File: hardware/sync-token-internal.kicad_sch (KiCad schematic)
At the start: 6 parts, among them U1 74AHC74D,118, U2 SN74LV1T125DBVRG4, U3 SN74LV1T125DBVRG4

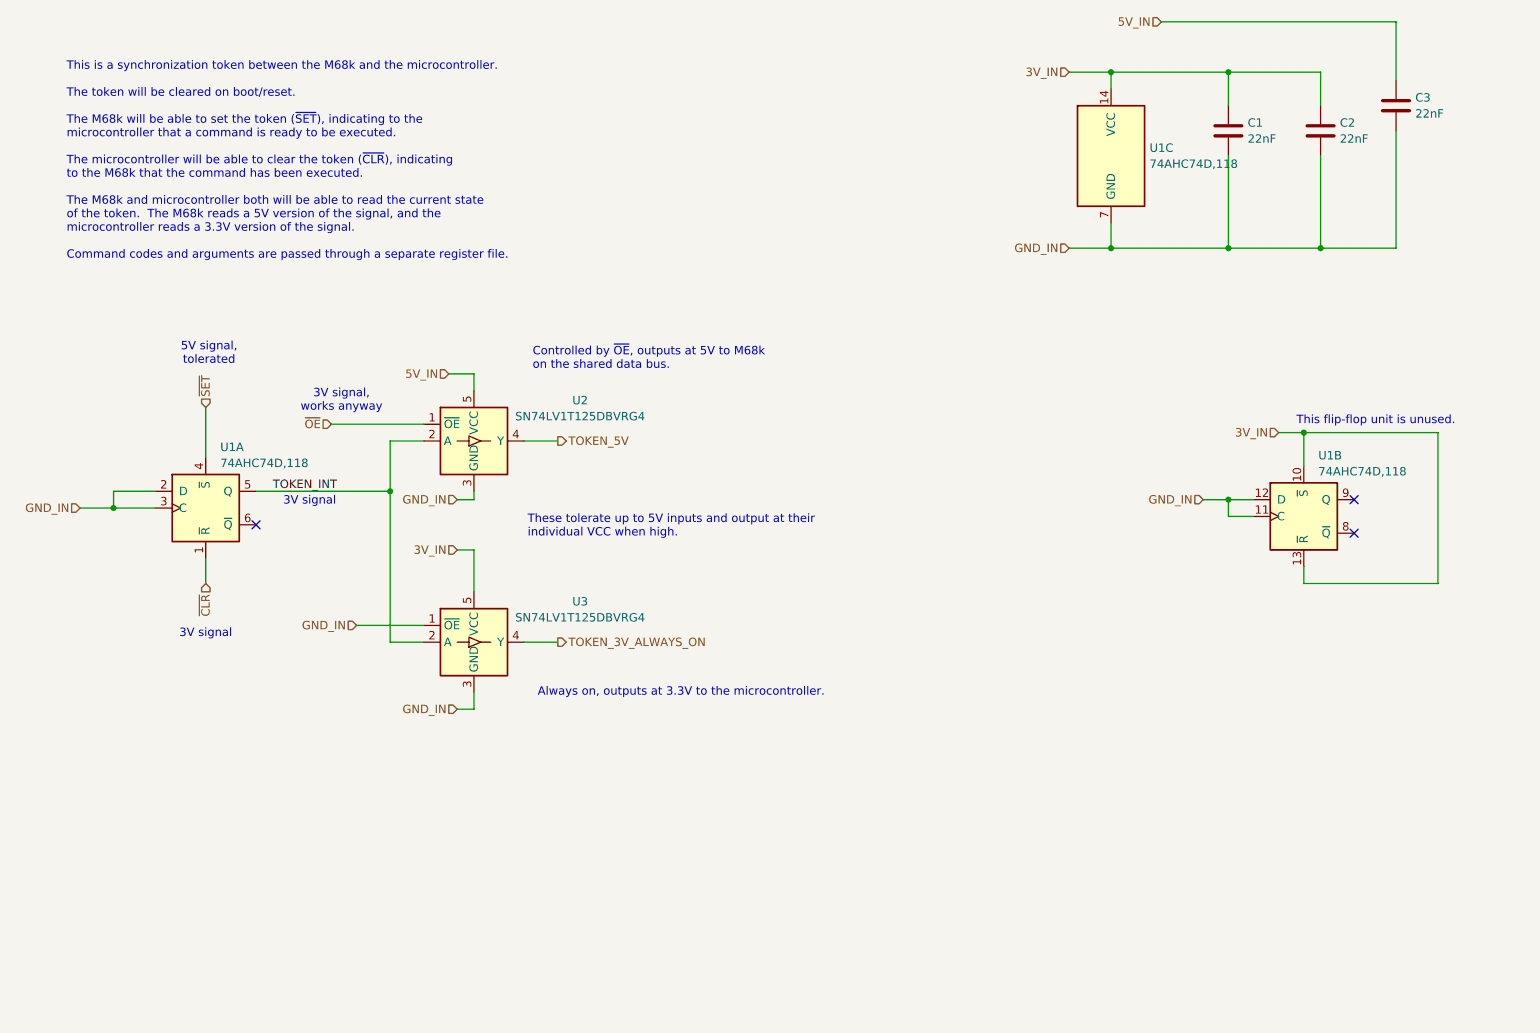
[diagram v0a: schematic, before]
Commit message: Massively reorganize board designs
Now planning to have most assembly done by JLCPCB, so trace sizes,
part selections, etc. are set accordingly.

New boards are:
 - cartridge interface & flash
 - microcontroller & registers
 - sram x2
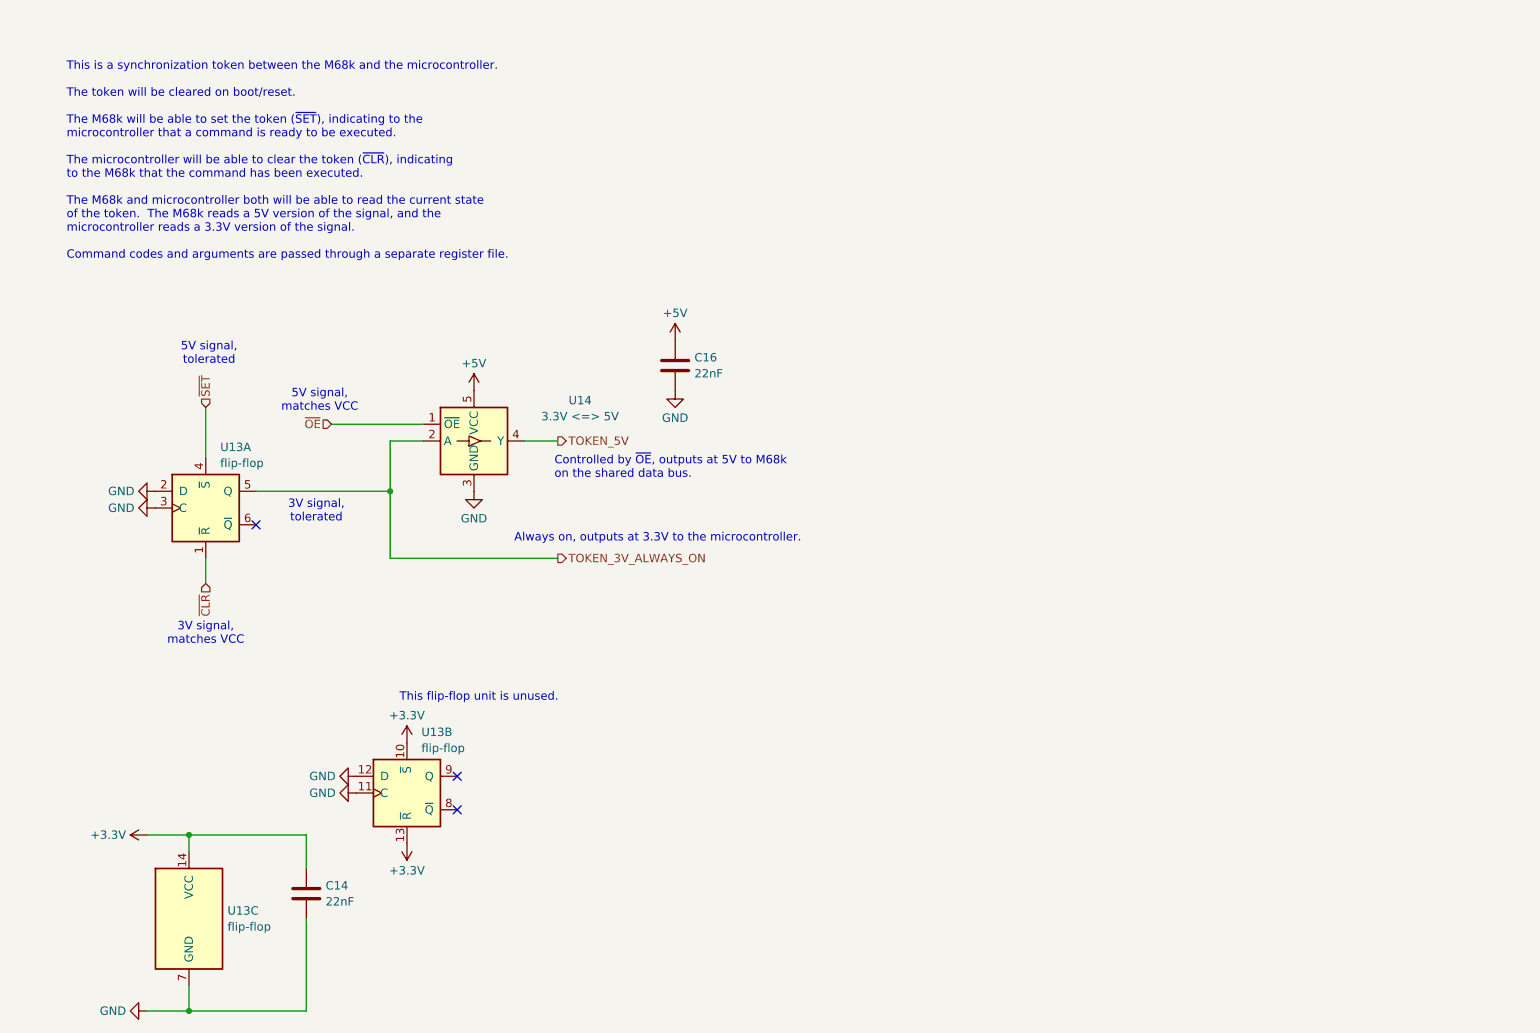
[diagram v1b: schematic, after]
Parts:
- removed C2: 22nF, Capacitor_SMD:C_0603_1608Metric, symbol Device:C
- removed U3: SN74LV1T125DBVRG4, Package_TO_SOT_SMD:SOT-23-5, symbol Logic_LevelTranslator:SN74LV1T125DBV
- C14: renamed from C1; JLCPCB Part Number (none) -> C21122; Mouser Part Number (none) -> 187-CL10B223KB8NNNC; Part Number (none) -> CL10B223KB8NNNC
- C16: renamed from C3; JLCPCB Part Number (none) -> C21122; Mouser Part Number (none) -> 187-CL10B223KB8NNNC; Part Number (none) -> CL10B223KB8NNNC
- U13: renamed from U1; value 74AHC74D,118 -> flip-flop; footprint Package_SO:SO-14_3.9x8.65mm_P1.27mm -> Package_SO:TSSOP-14_4.4x5mm_P0.65mm; JLCPCB Part Number (none) -> C71900; Mouser Part Number (none) -> 771-AHCPW118; Part Number (none) -> 74AHC74PW,118
- U14: renamed from U2; value SN74LV1T125DBVRG4 -> 3.3V <=> 5V; JLCPCB Part Number (none) -> C2675706; Mouser Part Number (none) -> 595-74LV1T125DBVRG4; Part Number (none) -> SN74LV1T125DBVRG4
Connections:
- net TOKEN_INT is gone; now on net TOKEN_3V_ALWAYS_ON: U13.5 (Q), U14.2 (A)
- net 3V_IN renamed +3.3V
- net 5V_IN renamed +5V
- net GND_IN renamed GND
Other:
- note added: "3V signal, matches VCC"
- note added: "3V signal, tolerated"
- note added: "5V signal, matches VCC"
- note removed: "3V signal"
- note removed: "3V signal, works anyway"
- note removed: "These tolerate up to 5V inputs and output at their individual VCC when high."
- moved on the sheet: C14, C16, U13B, U13C

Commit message: Add second sync bit to flag errors back to the Sega
Also split firmware speed tests out into their own file
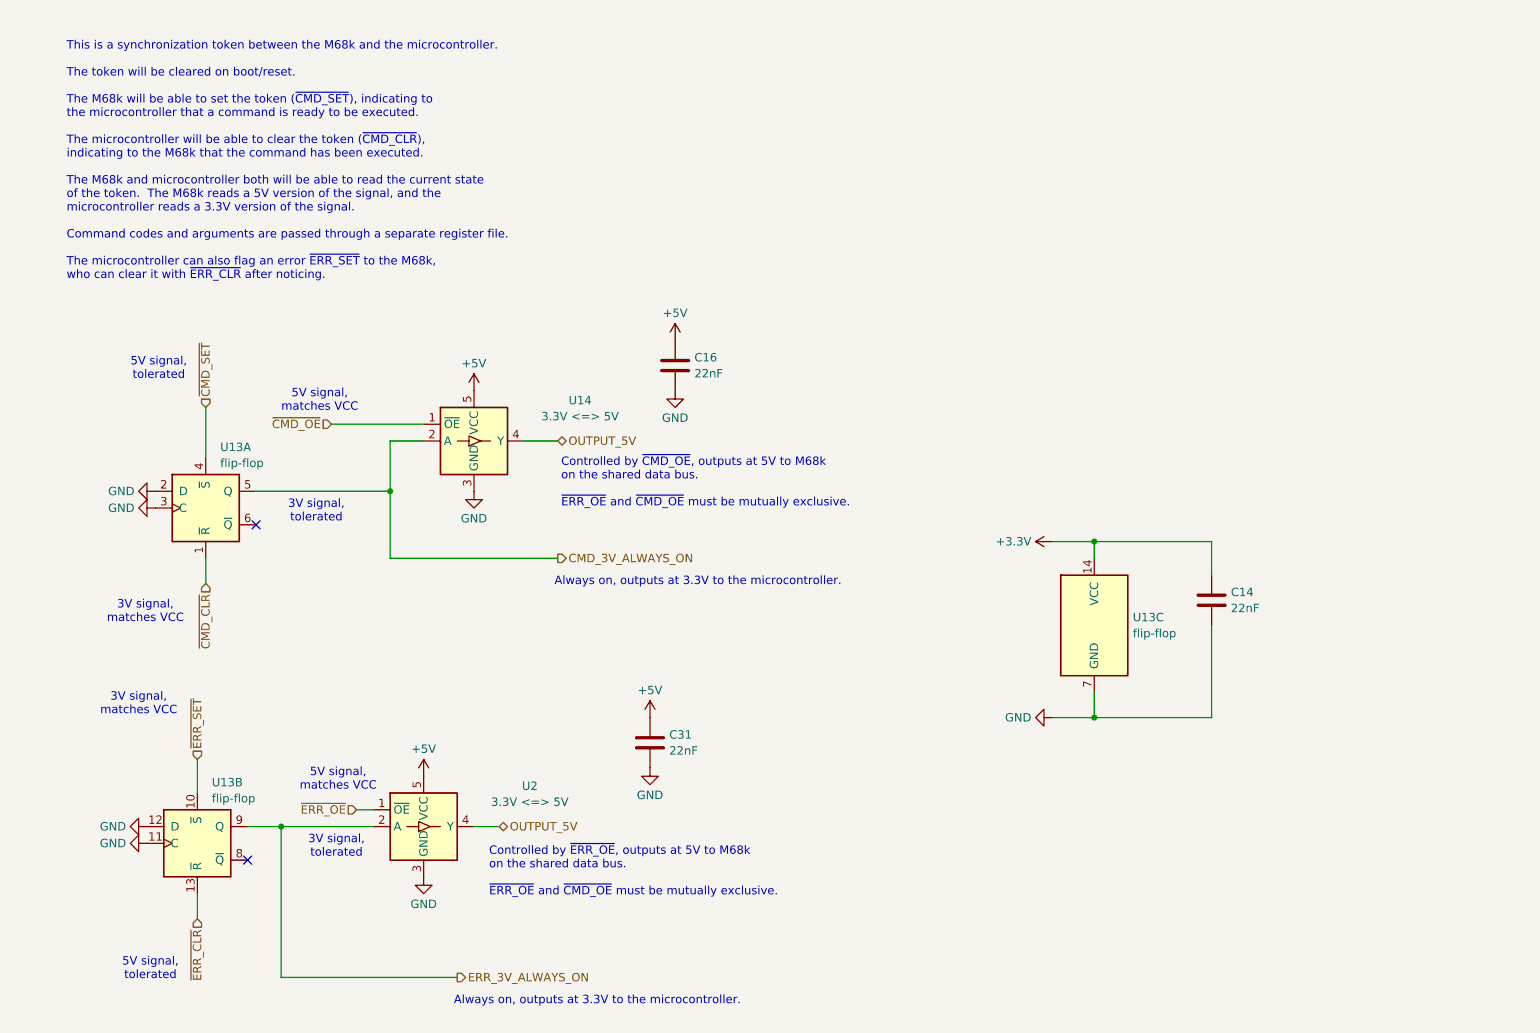
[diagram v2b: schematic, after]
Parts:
- added C31: 22nF, Capacitor_SMD:C_0603_1608Metric, symbol Device:C
- added U2: 3.3V <=> 5V, Package_TO_SOT_SMD:SOT-23-5, symbol Logic_LevelTranslator:SN74LV1T125DBV
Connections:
- net +3.3V: no longer U13.10 (~{S}), U13.13 (~{R})
- net +5V: now also C31.1, U2.5 (VCC)
- net GND: now also C31.2, U2.3 (GND)
- net ERR_3V_ALWAYS_ON: now reaches U13.9 (Q)
- net ERR_3V_ALWAYS_ON: now also U2.2 (A)
- net TOKEN_3V_ALWAYS_ON renamed CMD_3V_ALWAYS_ON
- net TOKEN_5V renamed OUTPUT_5V
- net OUTPUT_5V: now also U2.4 (Y)
- net ~{CLR} renamed ~{CMD_CLR}
- net ~{OE} renamed ~{CMD_OE}
- net ~{SET} renamed ~{CMD_SET}
- new net ~{ERR_CLR}: U13.13 (~{R})
- new net ~{ERR_OE}: U2.1 (~{OE})
- new net ~{ERR_SET}: U13.10 (~{S})
- no-connect marks 3 -> 2
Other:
- note added: "Controlled by ~{CMD_OE}, outputs at 5V to M68k on the shared data bus. ~{ERR_OE} and ~{CMD_OE} must be mutually exclusive."
- note added: "Controlled by ~{ERR_OE}, outputs at 5V to M68k on the shared data bus. ~{ERR_OE} and ~{CMD_OE} must be mutually exclusive."
- note added: "This is a synchronization token between the M68k and the microcontroller. The token will be cleared on boot/reset. The M68k will be able to set the token (~{CMD_SET}), indicating to the microcontroller that a command is ready to be executed. The microcontroller will be able to clear the token (~{CMD_CLR}), indicating to the M68k that the command has been executed. The M68k and microcontroller bot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"
- note removed: "Controlled by ~{OE}, outputs at 5V to M68k on the shared data bus."
- note removed: "This flip-flop unit is unused."
- note removed: "This is a synchronization token between the M68k and the microcontroller. The token will be cleared on boot/reset. The M68k will be able to set the token (~{SET}), indicating to the microcontroller that a command is ready to be executed. The microcontroller will be able to clear the token (~{CLR}), indicating to the M68k that the command has been executed. The M68k and microcontroller both will b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"
- moved on the sheet: C14, U13B, U13C

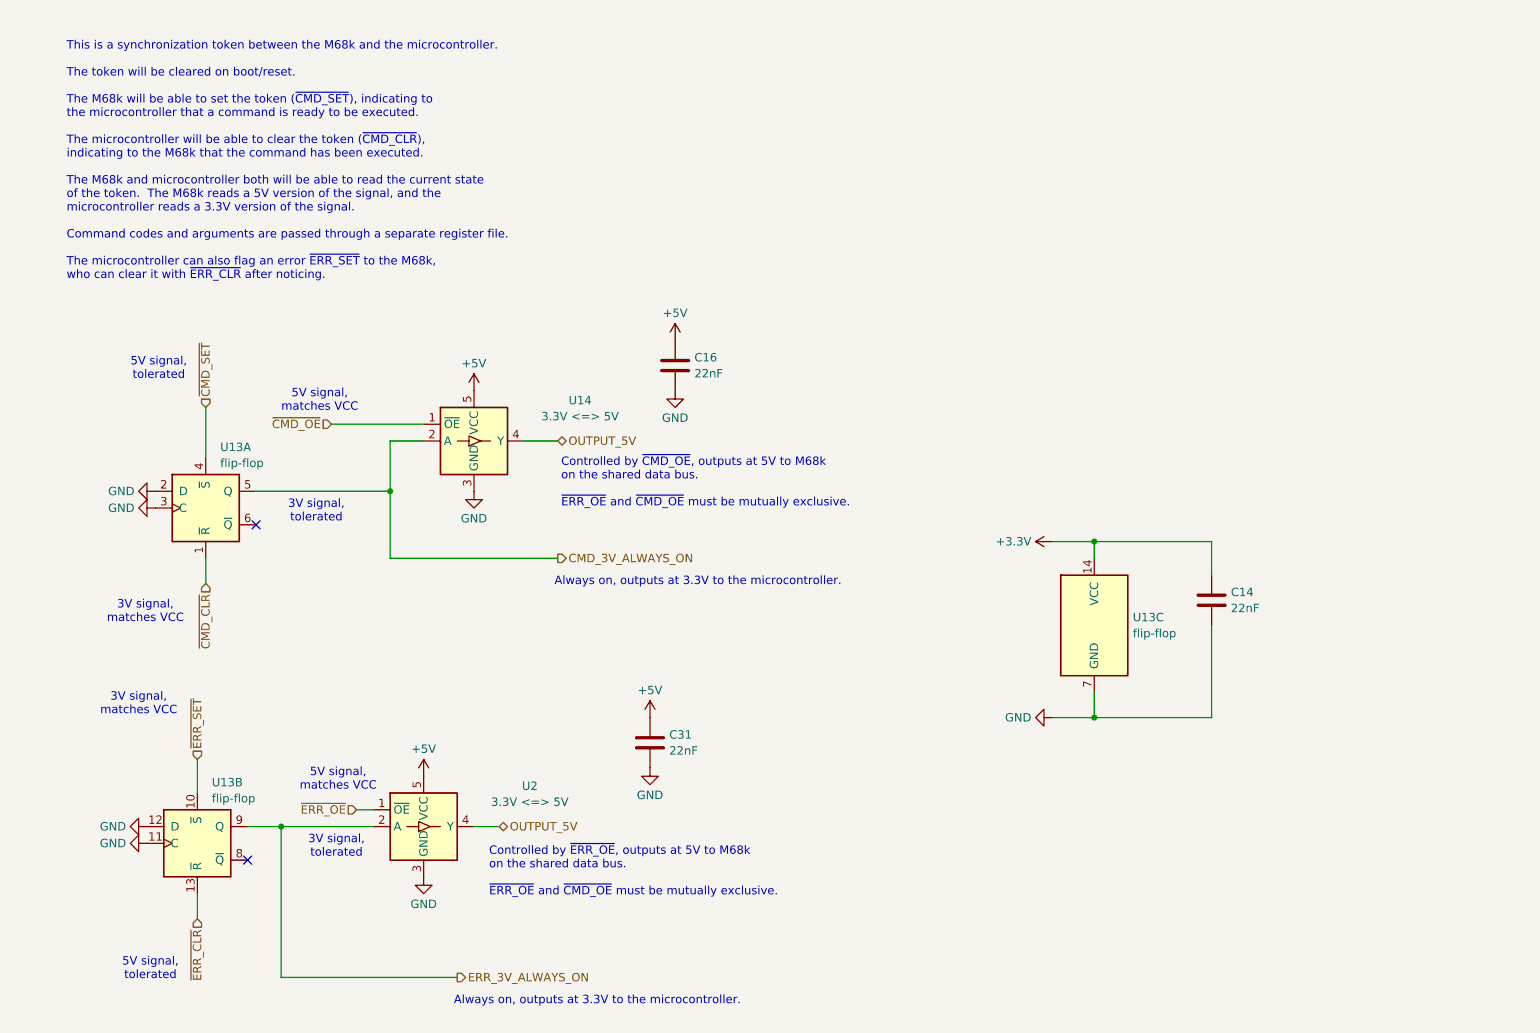
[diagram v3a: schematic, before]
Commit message: Revise microcontroller board based on latest cart board improvements
 - Update comments
 - Segregate the Ethernet module's power supply so it can be
   disconnected if something goes wrong in a prototype
 - Update board setup to match latest cart board
 - Remove unnecessary level-shifter
 - Fix address decoder to non-latching version
 - Fix address decoder output assignment
 - Consolidate buffer ICs in register file
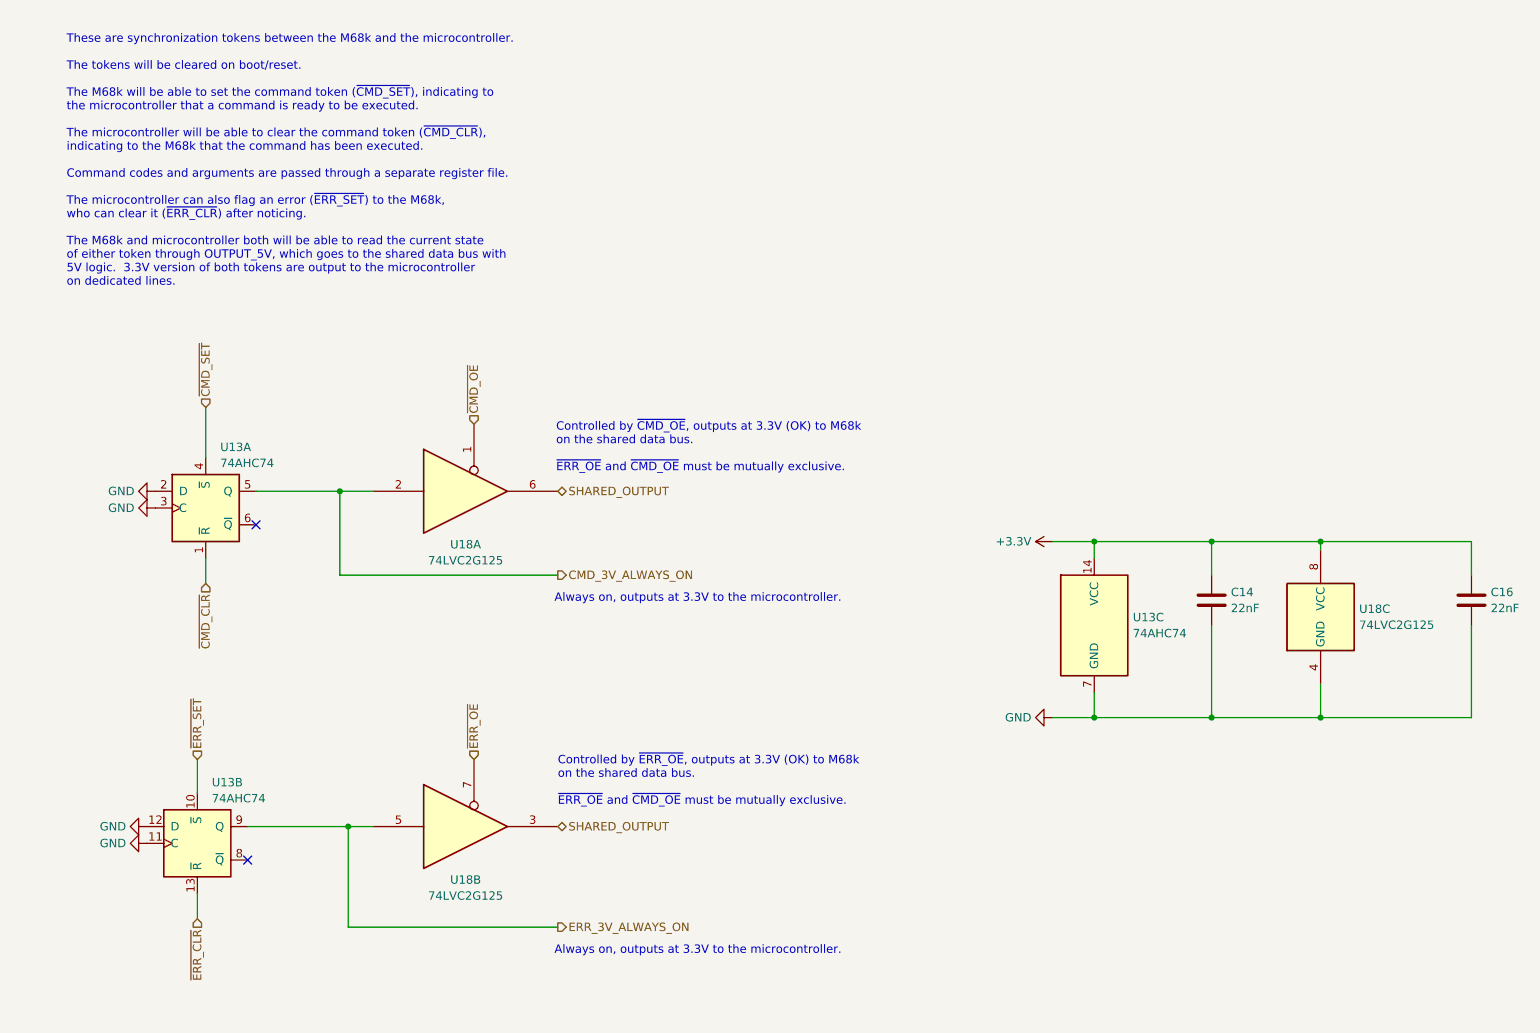
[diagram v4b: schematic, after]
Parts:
- removed C31: 22nF, Capacitor_SMD:C_0603_1608Metric, symbol Device:C
- removed U14, U2: 3.3V <=> 5V, Package_TO_SOT_SMD:SOT-23-5, symbol Logic_LevelTranslator:SN74LV1T125DBV
- added U18: 74LVC2G125, Package_SO:VSSOP-8_2.3x2mm_P0.5mm, symbol 74xGxx:74LVC2G125
- U13: value flip-flop -> 74AHC74
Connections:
- net +5V is gone; now on net +3.3V: C16.1
- net +3.3V: now also U18.8 (VCC)
- net CMD_3V_ALWAYS_ON: now also U18.2
- net ERR_3V_ALWAYS_ON: now also U18.5
- net GND: now also U18.4 (GND)
- net ~{CMD_OE}: now also U18.1
- net ~{ERR_OE}: now also U18.7
- new net SHARED_OUTPUT: U18.3, U18.6
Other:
- note added: "Controlled by ~{CMD_OE}, outputs at 3.3V (OK) to M68k on the shared data bus. ~{ERR_OE} and ~{CMD_OE} must be mutually exclusive."
- note added: "Controlled by ~{ERR_OE}, outputs at 3.3V (OK) to M68k on the shared data bus. ~{ERR_OE} and ~{CMD_OE} must be mutually exclusive."
- note added: "These are synchronization tokens between the M68k and the microcontroller. The tokens will be cleared on boot/reset. The M68k will be able to set the command token (~{CMD_SET}), indicating to the microcontroller that a command is ready to be executed. The microcontroller will be able to clear the command token (~{CMD_CLR}), indicating to the M68k that the command has been executed. Command codes 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"
- note removed: "3V signal, matches VCC"
- note removed: "3V signal, tolerated"
- note removed: "5V signal, matches VCC"
- note removed: "5V signal, tolerated"
- note removed: "Controlled by ~{CMD_OE}, outputs at 5V to M68k on the shared data bus. ~{ERR_OE} and ~{CMD_OE} must be mutually exclusive."
- note removed: "Controlled by ~{ERR_OE}, outputs at 5V to M68k on the shared data bus. ~{ERR_OE} and ~{CMD_OE} must be mutually exclusive."
- note removed: "This is a synchronization token between the M68k and the microcontroller. The token will be cleared on boot/reset. The M68k will be able to set the token (~{CMD_SET}), indicating to the microcontroller that a command is ready to be executed. The microcontroller will be able to clear the token (~{CMD_CLR}), indicating to the M68k that the command has been executed. The M68k and microcontroller bot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"
- moved on the sheet: C16
